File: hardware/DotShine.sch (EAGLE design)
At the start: 63 parts, among them CN1 1X4-BIG, IC1 CAT24M010TS, IC3 SI1145, J3 USB-MICROB, U1 ATMEGA328P-MU-QFN32, U2 TMP102, U3 ATSHA204-TSU, U4 JDY-16, X2 MC-RTC-RV-4162-C7-I2C

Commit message: SJ on PWR led
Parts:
- added J6: (no value), solderjumper:SOLDERJUMPER.2.MED
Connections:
- new net N$34: J6.2, LED2.A
- net USB_FOR_LED: now also J6.1; no longer LED2.A
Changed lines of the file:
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@@
 <part name="+3V23" library="supply1" deviceset="+3V3" device=""/>
 <part name="J5" library="solderjumper" deviceset="SOLDERJUMPER.2" device=".MED"/>
+<part name="J6" library="solderjumper" deviceset="SOLDERJUMPER.2" device=".MED"/>
 </parts>
 <sheets>
@@
 <instance part="+3V23" gate="G$1" x="111.76" y="-400.05" rot="R90"/>
 <instance part="J5" gate="G$1" x="241.3" y="-299.72"/>
+<instance part="J6" gate="G$1" x="129.54" y="142.24"/>
 </instances>
 <busses>
@@
 </segment>
 <segment>
-<pinref part="LED2" gate="G$1" pin="A"/>
-<wire x1="134.62" y1="142.24" x2="123.19" y2="142.24" width="0.1524" layer="91"/>
-<label x="123.19" y="142.24" size="1.27" layer="95" rot="R180" xref="yes"/>
+<wire x1="127" y1="142.24" x2="106.68" y2="142.24" width="0.1524" layer="91"/>
+<label x="106.68" y="142.24" size="1.27" layer="95" rot="R180" xref="yes"/>
+<pinref part="J6" gate="G$1" pin="1"/>
 </segment>
 </net>
@@
 </segment>
 </net>
+<net name="N$34" class="0">
+<segment>
+<pinref part="LED2" gate="G$1" pin="A"/>
+<pinref part="J6" gate="G$1" pin="2"/>
+<wire x1="134.62" y1="142.24" x2="132.08" y2="142.24" width="0.1524" layer="91"/>
+</segment>
+</net>

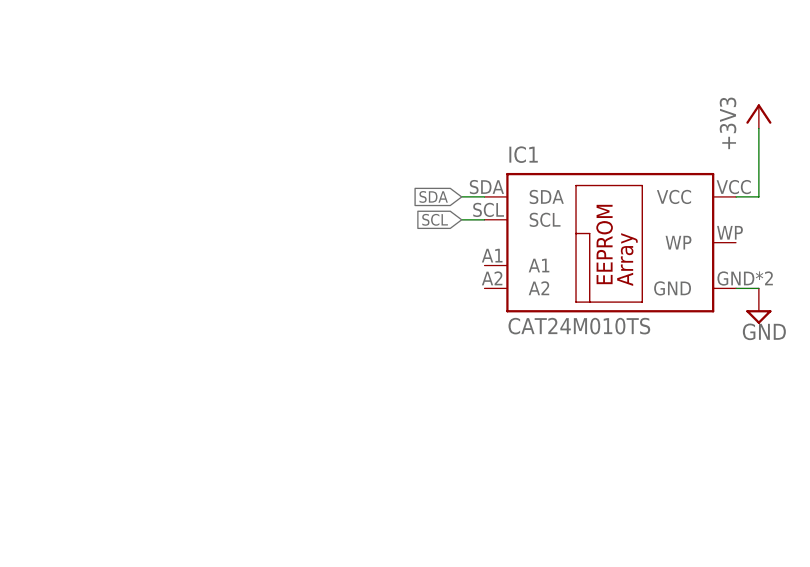
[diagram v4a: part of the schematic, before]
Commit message: Connect E2PROM A1 to 3V3, avoid collision with BLE
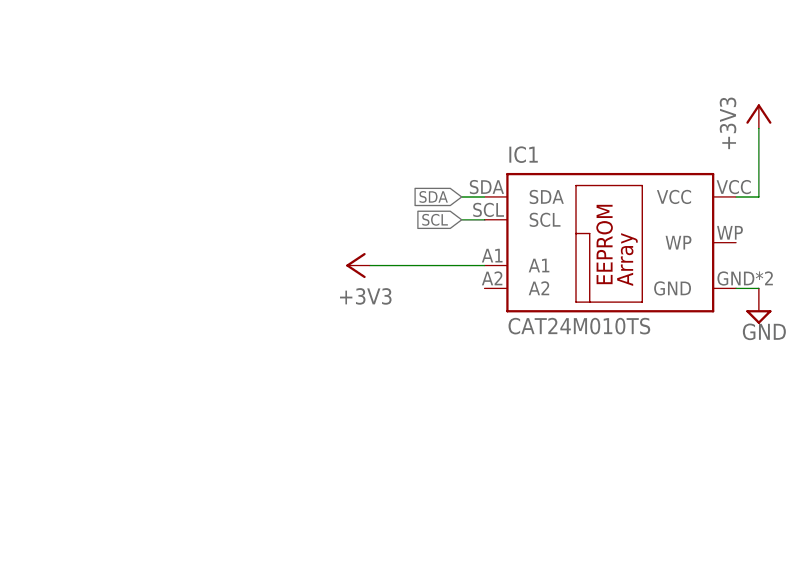
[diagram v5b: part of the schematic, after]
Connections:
- net +3V3: now also IC1.A1
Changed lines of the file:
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@@
 <part name="J5" library="solderjumper" deviceset="SOLDERJUMPER.2" device=".MED"/>
 <part name="J6" library="solderjumper" deviceset="SOLDERJUMPER.2" device=".MED"/>
+<part name="+3V24" library="supply1" deviceset="+3V3" device=""/>
 </parts>
 <sheets>
@@
 <instance part="J5" gate="G$1" x="241.3" y="-299.72"/>
 <instance part="J6" gate="G$1" x="129.54" y="142.24"/>
+<instance part="+3V24" gate="G$1" x="66.04" y="-165.1" rot="R90"/>
 </instances>
 <busses>
@@
 <wire x1="129.54" y1="-400.05" x2="114.3" y2="-400.05" width="0.1524" layer="91"/>
 </segment>
-</net>
+<segment>
+<pinref part="IC1" gate="G$1" pin="A1"/>
+<pinref part="+3V24" gate="G$1" pin="+3V3"/>
+<wire x1="81.28" y1="-165.1" x2="68.58" y2="-165.1" width="0.1524" layer="91"/>
+</segment>
+</net>

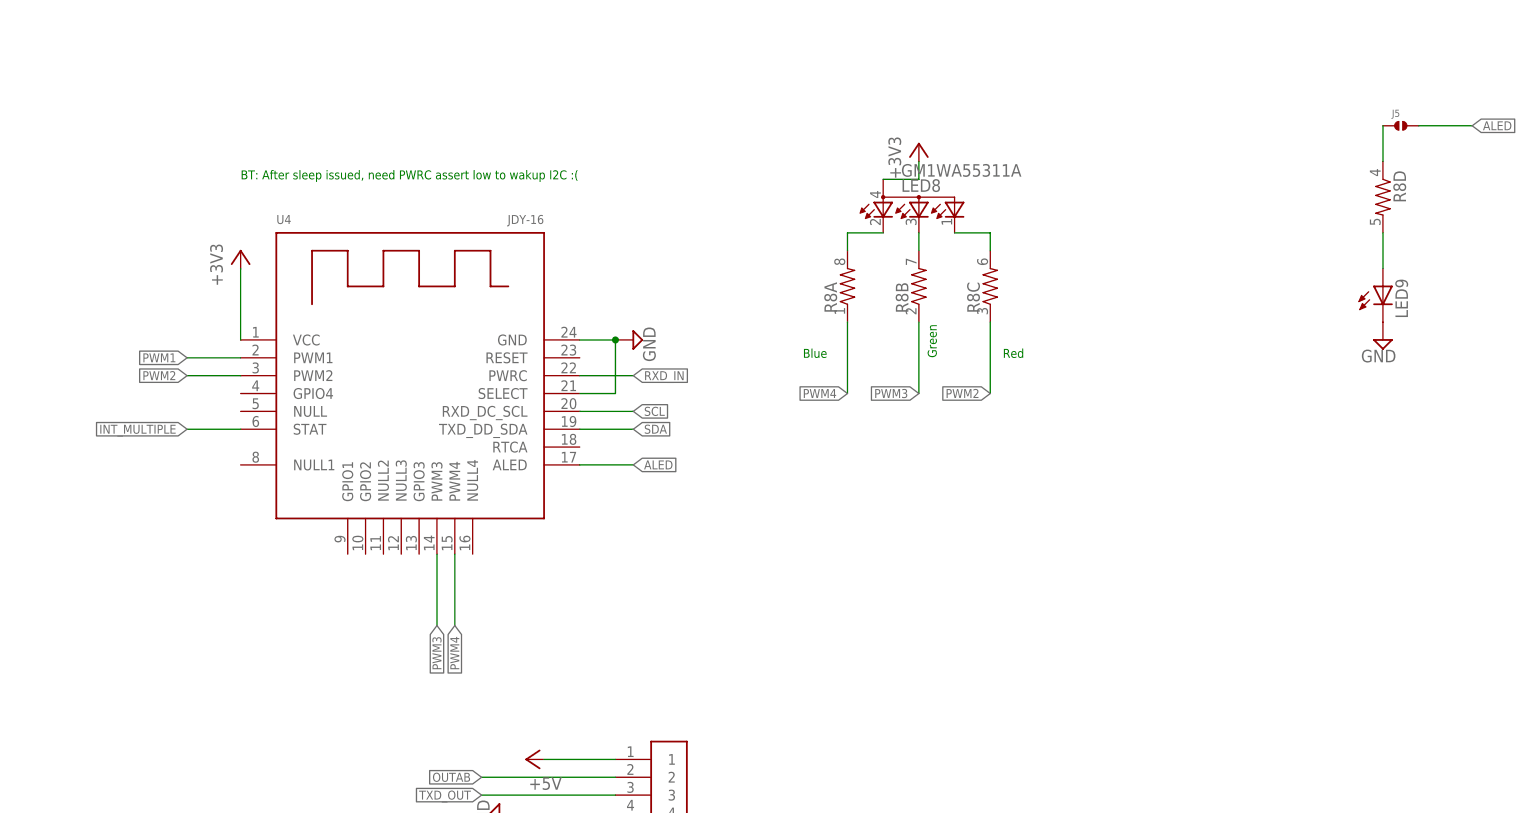
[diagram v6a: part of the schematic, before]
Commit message: Remove BLE RGB
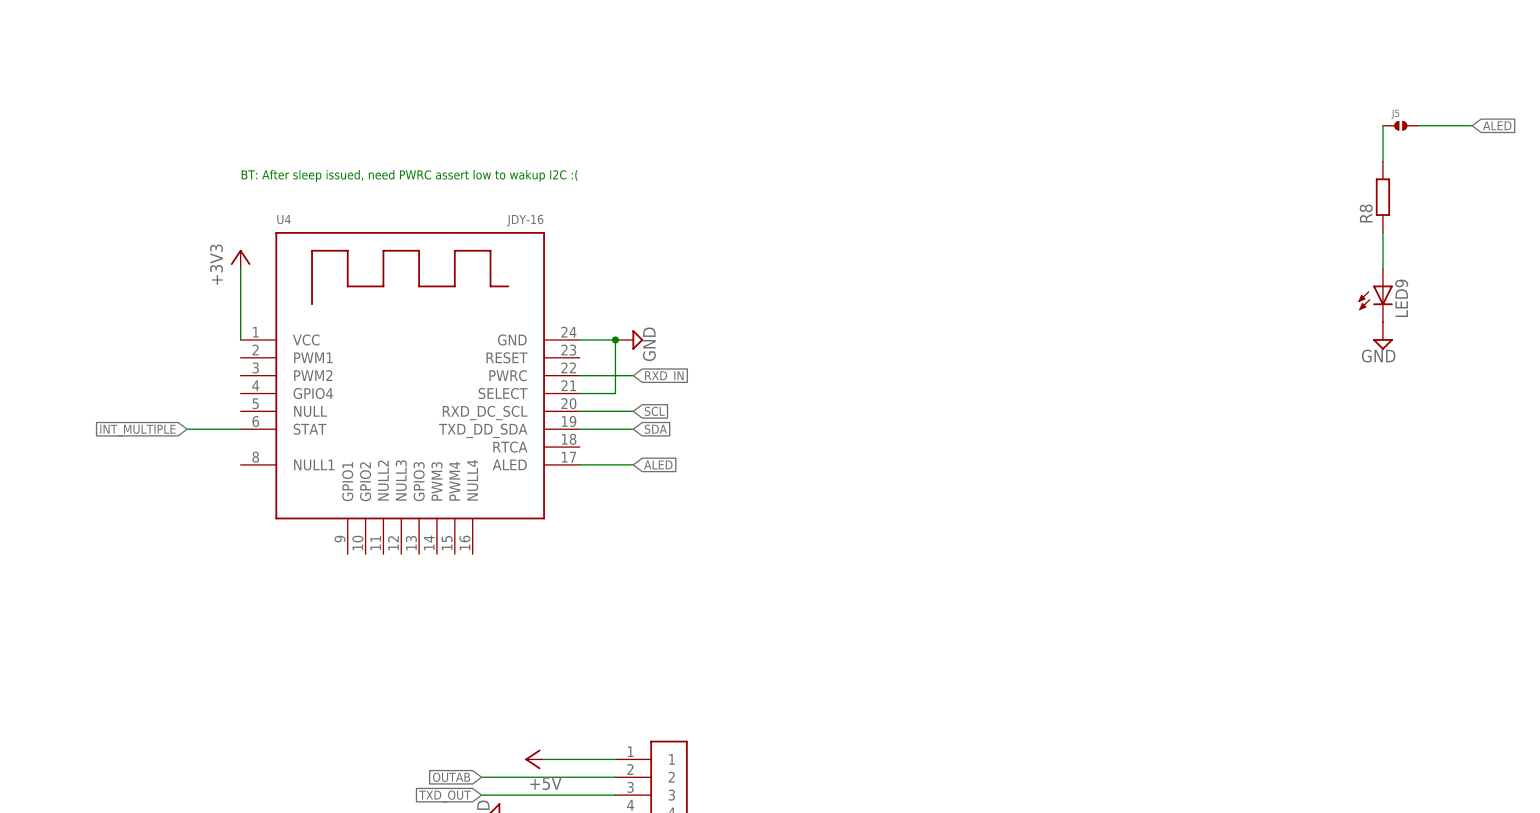
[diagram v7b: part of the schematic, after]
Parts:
- removed LED8: GM1WA55311A, led:GM1WA55311A
- R8: device SparkFun:RESISTOR-ARRAY0603-ARV -> rcl:R-EU_R0603
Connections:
- removed net BT_BLUE: LED8.CRED, R8A.2
- removed net BT_GREEN: LED8.CBLUE, R8B.2
- removed net N$1: LED8.CGREEN, R8C.2
- removed net PWM1: U4.PWM1
- removed net PWM2: R8C.1, U4.PWM2
- removed net PWM3: R8B.1, U4.PWM3
- removed net PWM4: R8A.1, U4.PWM4
- net +3V3: no longer LED8.A
- net N$2: now also R8.2; no longer R8D.1
- net N$4: now also R8.1; no longer R8D.2
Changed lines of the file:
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@@
 <setting verticaltext="up"/>
 </settings>
-<grid distance="0.05" unitdist="inch" unit="inch" style="lines" multiple="1" display="no" altdistance="0.01" altunitdist="inch" altunit="inch"/>
+<grid distance="0.1" unitdist="inch" unit="inch" style="lines" multiple="1" display="no" altdistance="0.01" altunitdist="inch" altunit="inch"/>
 <layers>
 <layer number="1" name="Top" color="4" fill="1" visible="no" active="no"/>
@@
 <part name="SUPPLY1" library="supply2" deviceset="GND" device=""/>
 <part name="U4" library="altro" deviceset="JDY-16" device=""/>
-<part name="+3V18" library="supply1" deviceset="+3V3" device=""/>
-<part name="LED8" library="led" deviceset="GM1WA55311A" device=""/>
 <part name="LED9" library="SparkFun" deviceset="LED" device="0603"/>
 <part name="SUPPLY8" library="supply2" deviceset="GND" device=""/>
-<part name="R8" library="SparkFun" deviceset="RESISTOR-ARRAY" device="0603-ARV"/>
 <part name="SUPPLY9" library="supply2" deviceset="GND" device=""/>
 <part name="+3V22" library="supply1" deviceset="+3V3" device=""/>
@@
 <part name="+3V24" library="supply1" deviceset="+3V3" device=""/>
 <part name="U$4" library="mihai_connectors_jst" deviceset="JST-8" device=""/>
+<part name="R8" library="rcl" library_urn="urn:adsk.eagle:library:334" deviceset="R-EU_" device="R0603" package3d_urn="urn:adsk.eagle:package:23555/2"/>
 </parts>
 <sheets>
@@
 leakage current too high </text>
 <text x="124.46" y="-147.32" size="1.27" layer="91">HW Reset with SW</text>
-<text x="175.26" y="-332.74" size="1.27" layer="91" rot="R90">Green</text>
-<text x="184.658" y="-332.74" size="1.27" layer="91">Red</text>
-<text x="156.21" y="-332.74" size="1.27" layer="91">Blue</text>
 <text x="76.2" y="-307.34" size="1.27" layer="91">BT: After sleep issued, need PWRC assert low to wakup I2C :(</text>
 </plain>
@@
 <instance part="SUPPLY1" gate="GND" x="162.56" y="119.38" rot="R90"/>
 <instance part="U4" gate="G$1" x="101.6" y="-337.82"/>
-<instance part="+3V18" gate="G$1" x="172.72" y="-302.26"/>
-<instance part="LED8" gate="G$1" x="172.72" y="-309.88"/>
 <instance part="LED9" gate="G$1" x="238.76" y="-322.58"/>
 <instance part="SUPPLY8" gate="GND" x="238.76" y="-330.2" rot="MR0"/>
-<instance part="R8" gate="A" x="162.56" y="-322.58" rot="R90"/>
-<instance part="R8" gate="B" x="172.72" y="-322.58" rot="R90"/>
-<instance part="R8" gate="C" x="182.88" y="-322.58" rot="R90"/>
-<instance part="R8" gate="D" x="238.76" y="-309.88" rot="R270"/>
 <instance part="SUPPLY9" gate="GND" x="132.08" y="-330.2" rot="MR270"/>
 <instance part="+3V22" gate="G$1" x="76.2" y="-317.5"/>
@@
 <instance part="+3V24" gate="G$1" x="66.04" y="-165.1" rot="R90"/>
 <instance part="U$4" gate="G$1" x="134.62" y="-412.75"/>
+<instance part="R8" gate="G$1" x="238.76" y="-309.88" rot="R90"/>
 </instances>
 <busses>
@@
 </segment>
 <segment>
-<pinref part="LED8" gate="G$1" pin="A"/>
-<pinref part="+3V18" gate="G$1" pin="+3V3"/>
-<wire x1="167.64" y1="-307.34" x2="172.72" y2="-307.34" width="0.1524" layer="91"/>
-<wire x1="172.72" y1="-307.34" x2="172.72" y2="-304.8" width="0.1524" layer="91"/>
-</segment>
-<segment>
 <pinref part="+3V22" gate="G$1" pin="+3V3"/>
 <pinref part="U4" gate="G$1" pin="VCC"/>
@@
 </segment>
 </net>
-<net name="BT_GREEN" class="0">
-<segment>
-<pinref part="LED8" gate="G$1" pin="CBLUE"/>
-<pinref part="R8" gate="B" pin="2"/>
-<wire x1="172.72" y1="-317.5" x2="172.72" y2="-314.96" width="0.1524" layer="91"/>
-</segment>
-</net>
-<net name="BT_BLUE" class="0">
-<segment>
-<pinref part="LED8" gate="G$1" pin="CRED"/>
-<pinref part="R8" gate="A" pin="2"/>
-<wire x1="167.64" y1="-314.96" x2="162.56" y2="-314.96" width="0.1524" layer="91"/>
-<wire x1="162.56" y1="-314.96" x2="162.56" y2="-317.5" width="0.1524" layer="91"/>
-</segment>
-</net>
-<net name="PWM1" class="0">
-<segment>
-<pinref part="U4" gate="G$1" pin="PWM1"/>
-<wire x1="76.2" y1="-332.74" x2="68.58" y2="-332.74" width="0.1524" layer="91"/>
-<label x="68.58" y="-332.74" size="1.27" layer="95" rot="R180" xref="yes"/>
-</segment>
-</net>
-<net name="PWM2" class="0">
-<segment>
-<pinref part="U4" gate="G$1" pin="PWM2"/>
-<wire x1="76.2" y1="-335.28" x2="68.58" y2="-335.28" width="0.1524" layer="91"/>
-<label x="68.58" y="-335.28" size="1.27" layer="95" rot="R180" xref="yes"/>
-</segment>
-<segment>
-<pinref part="R8" gate="C" pin="1"/>
-<wire x1="182.88" y1="-327.66" x2="182.88" y2="-337.82" width="0.1524" layer="91"/>
-<label x="182.88" y="-337.82" size="1.27" layer="95" rot="R180" xref="yes"/>
-</segment>
-</net>
-<net name="PWM3" class="0">
-<segment>
-<pinref part="U4" gate="G$1" pin="PWM3"/>
-<wire x1="104.14" y1="-360.68" x2="104.14" y2="-370.84" width="0.1524" layer="91"/>
-<label x="104.14" y="-370.84" size="1.27" layer="95" rot="R270" xref="yes"/>
-</segment>
-<segment>
-<pinref part="R8" gate="B" pin="1"/>
-<wire x1="172.72" y1="-327.66" x2="172.72" y2="-337.82" width="0.1524" layer="91"/>
-<label x="172.72" y="-337.82" size="1.27" layer="95" rot="R180" xref="yes"/>
-</segment>
-</net>
-<net name="PWM4" class="0">
-<segment>
-<pinref part="U4" gate="G$1" pin="PWM4"/>
-<wire x1="106.68" y1="-360.68" x2="106.68" y2="-370.84" width="0.1524" layer="91"/>
-<label x="106.68" y="-370.84" size="1.27" layer="95" rot="R270" xref="yes"/>
-</segment>
-<segment>
-<pinref part="R8" gate="A" pin="1"/>
-<wire x1="162.56" y1="-327.66" x2="162.56" y2="-337.82" width="0.1524" layer="91"/>
-<label x="162.56" y="-337.82" size="1.27" layer="95" rot="R180" xref="yes"/>
-</segment>
-</net>
 <net name="ALED" class="0">
 <segment>
@@
 <net name="N$4" class="0">
 <segment>
-<pinref part="R8" gate="D" pin="2"/>
 <pinref part="LED9" gate="G$1" pin="A"/>
 <wire x1="238.76" y1="-314.96" x2="238.76" y2="-320.04" width="0.1524" layer="91"/>
-</segment>
-</net>
-<net name="N$1" class="0">
-<segment>
-<pinref part="LED8" gate="G$1" pin="CGREEN"/>
-<pinref part="R8" gate="C" pin="2"/>
-<wire x1="177.8" y1="-314.96" x2="182.88" y2="-314.96" width="0.1524" layer="91"/>
-<wire x1="182.88" y1="-314.96" x2="182.88" y2="-317.5" width="0.1524" layer="91"/>
+<pinref part="R8" gate="G$1" pin="1"/>
 </segment>
 </net>
@@
 <segment>
 <pinref part="J5" gate="G$1" pin="1"/>
-<pinref part="R8" gate="D" pin="1"/>
 <wire x1="238.76" y1="-299.72" x2="238.76" y2="-304.8" width="0.1524" layer="91"/>
+<pinref part="R8" gate="G$1" pin="2"/>
 </segment>
 </net>
@@
 which will not be processed correctly with this version.
 </note>
+<note version="8.2" severity="warning">
+Since Version 8.2, EAGLE supports online libraries. The ids
+of those online libraries will not be understood (or retained)
+with this version.
+</note>
 <note version="8.3" severity="warning">
 Since Version 8.3, EAGLE supports URNs for individual library
@@
 will not be understood (or retained) with this version.
 </note>
+<note version="8.3" severity="warning">
+Since Version 8.3, EAGLE supports the association of 3D packages
+with devices in libraries, schematics, and board files. Those 3D
+packages will not be understood (or retained) with this version.
+</note>
+<note version="8.4" severity="warning">
+Since Version 8.4, EAGLE supports properties for SPICE simulation.
+Probes in schematics and SPICE mapping objects found in parts and library devices
+will not be understood with this version. Update EAGLE to the latest version
+for full support of SPICE simulation.
+</note>
 </compatibility>

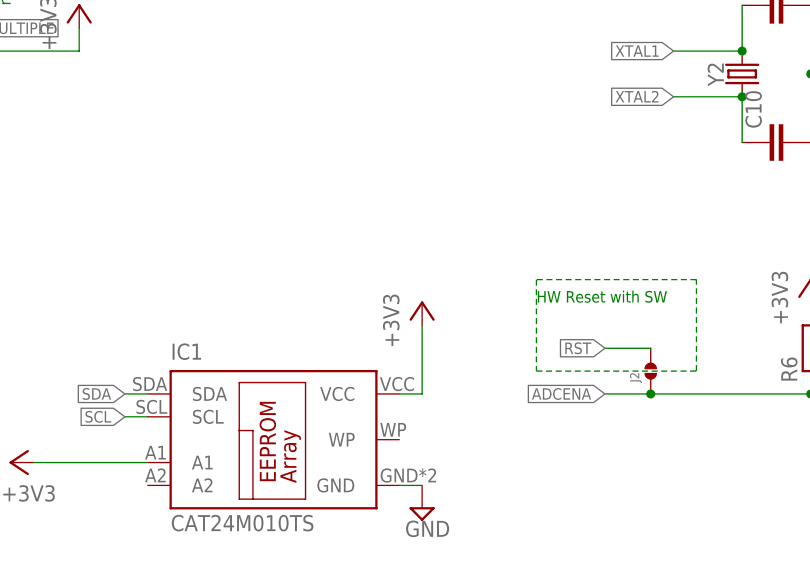
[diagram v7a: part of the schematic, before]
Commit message: I2C EEPROM Vdd controlled from MCU pin
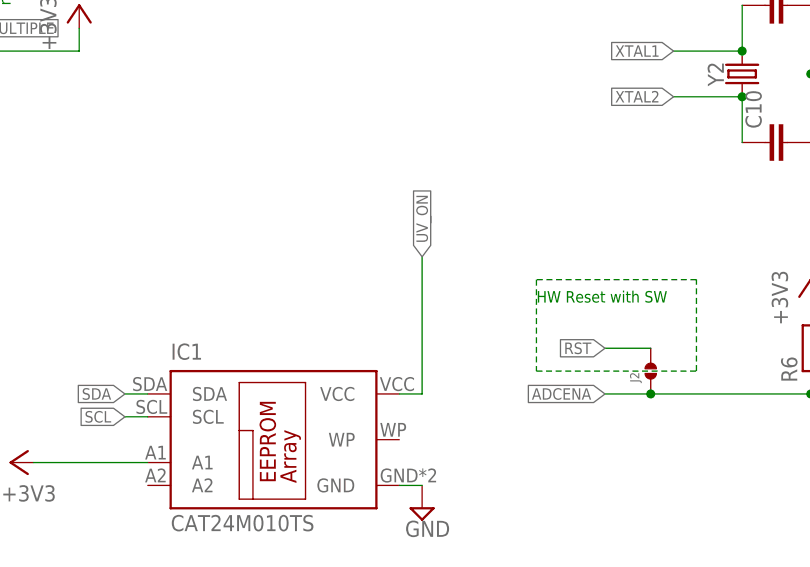
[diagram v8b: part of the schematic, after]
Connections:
- net +3V3: no longer IC1.VCC
- net UV_ON: now also IC1.VCC
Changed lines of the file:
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@@
 <part name="SUPPLY16" library="supply2" deviceset="GND" device=""/>
 <part name="IC1" library="CAT24M01YI" deviceset="CAT24M01" device="TS" technology="0"/>
-<part name="+3V9" library="supply1" deviceset="+3V3" device=""/>
 <part name="U3" library="SparkFun-IC-Special-Function" deviceset="ATSHA204" device="-TSU"/>
 <part name="+3V10" library="supply1" deviceset="+3V3" device=""/>
@@
 <instance part="SUPPLY16" gate="GND" x="111.76" y="-170.18"/>
 <instance part="IC1" gate="G$1" x="93.98" y="-162.56"/>
-<instance part="+3V9" gate="G$1" x="111.76" y="-147.32"/>
 <instance part="U3" gate="G$1" x="167.64" y="-157.48"/>
 <instance part="+3V10" gate="G$1" x="180.34" y="-152.4"/>
@@
 </segment>
 <segment>
-<wire x1="111.76" y1="-149.86" x2="111.76" y2="-157.48" width="0.1524" layer="91"/>
-<pinref part="IC1" gate="G$1" pin="VCC"/>
-<wire x1="111.76" y1="-157.48" x2="109.22" y2="-157.48" width="0.1524" layer="91"/>
-<pinref part="+3V9" gate="G$1" pin="+3V3"/>
-</segment>
-<segment>
 <pinref part="U3" gate="G$1" pin="VCC"/>
 <wire x1="175.26" y1="-154.94" x2="180.34" y2="-154.94" width="0.1524" layer="91"/>
@@
 <label x="167.64" y="-205.74" size="1.27" layer="95" rot="R180" xref="yes"/>
 </segment>
-</net>
+<segment>
+<pinref part="IC1" gate="G$1" pin="VCC"/>
+<wire x1="109.22" y1="-157.48" x2="111.76" y2="-157.48" width="0.1524" layer="91"/>
+<wire x1="111.76" y1="-157.48" x2="111.76" y2="-142.24" width="0.1524" layer="91"/>
+<label x="111.76" y="-142.24" size="1.27" layer="95" rot="R90" xref="yes"/>
+</segment>
+</net>
